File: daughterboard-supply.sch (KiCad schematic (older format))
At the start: 12 parts, among them J4 43045-1013, Q15 DMN4010LFG-7, U15 AP62301WU-7

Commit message: Loclib performed
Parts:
- Q15: footprint antmicro-footprints:POWERVDFN-8 -> nuc-compute-cluster-power-breakout-footprints:POWERVDFN-8; symbol antmicroTransistorsFETsMOSFETsSingle:DMN4010LFG-7 -> nuc-compute-cluster-power-breakout:DMN4010LFG-7
- R38, R39: footprint antmicro-footprints:0402-res -> nuc-compute-cluster-power-breakout-footprints:0402-res; symbol antmicroResistors0402:R_10k_0402 -> nuc-compute-cluster-power-breakout:R_10k_0402
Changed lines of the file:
@@
 DB_3V3
 $Comp
-L antmicroTransistorsFETsMOSFETsSingle:DMN4010LFG-7 Q15
+L nuc-compute-cluster-power-breakout:DMN4010LFG-7 Q15
 U 1 1 626C5C42
 P 3525 3950
 F 0 "Q15" V 3861 3950 79  0000 C CNN
 F 1 "DMN4010LFG-7" V 3726 3950 79  0000 C CNN
-F 2 "antmicro-footprints:POWERVDFN-8" H 3525 3950 79  0001 C CNN
+F 2 "nuc-compute-cluster-power-breakout-footprints:POWERVDFN-8" H 3525 3950 79  0001 C CNN
 F 3 "https://www.diodes.com/assets/Datasheets/DMN4010LFG.pdf" H 3525 3950 79  0001 C CNN
 F 4 "DMN4010LFG-7" H 3525 3950 79  0001 C CNN "MPN"
@@
 $EndComp
 $Comp
-L antmicroResistors0402:R_10k_0402 R38
+L nuc-compute-cluster-power-breakout:R_10k_0402 R38
 U 1 1 626D757A
 P 3625 4500
 F 0 "R38" V 3575 4325 60  0000 L CNN
 F 1 "R_10k_0402" H 3625 4350 60  0001 C CNN
-F 2 "antmicro-footprints:0402-res" H 3825 4700 60  0001 L CNN
+F 2 "nuc-compute-cluster-power-breakout-footprints:0402-res" H 3825 4700 60  0001 L CNN
 F 3 "" H 3625 4500 50  0001 C CNN
 F 4 "VISHAY" H 3825 4900 60  0001 L CNN "Manufacturer"
@@
 	3875 3925 4050 3925
 $Comp
-L antmicroResistors0402:R_10k_0402 R39
+L nuc-compute-cluster-power-breakout:R_10k_0402 R39
 U 1 1 626D93ED
 P 3875 4500
 F 0 "R39" V 3825 4575 60  0000 L CNN
 F 1 "R_10k_0402" H 3875 4350 60  0001 C CNN
-F 2 "antmicro-footprints:0402-res" H 4075 4700 60  0001 L CNN
+F 2 "nuc-compute-cluster-power-breakout-footprints:0402-res" H 4075 4700 60  0001 L CNN
 F 3 "" H 3875 4500 50  0001 C CNN
 F 4 "VISHAY" H 4075 4900 60  0001 L CNN "Manufacturer"

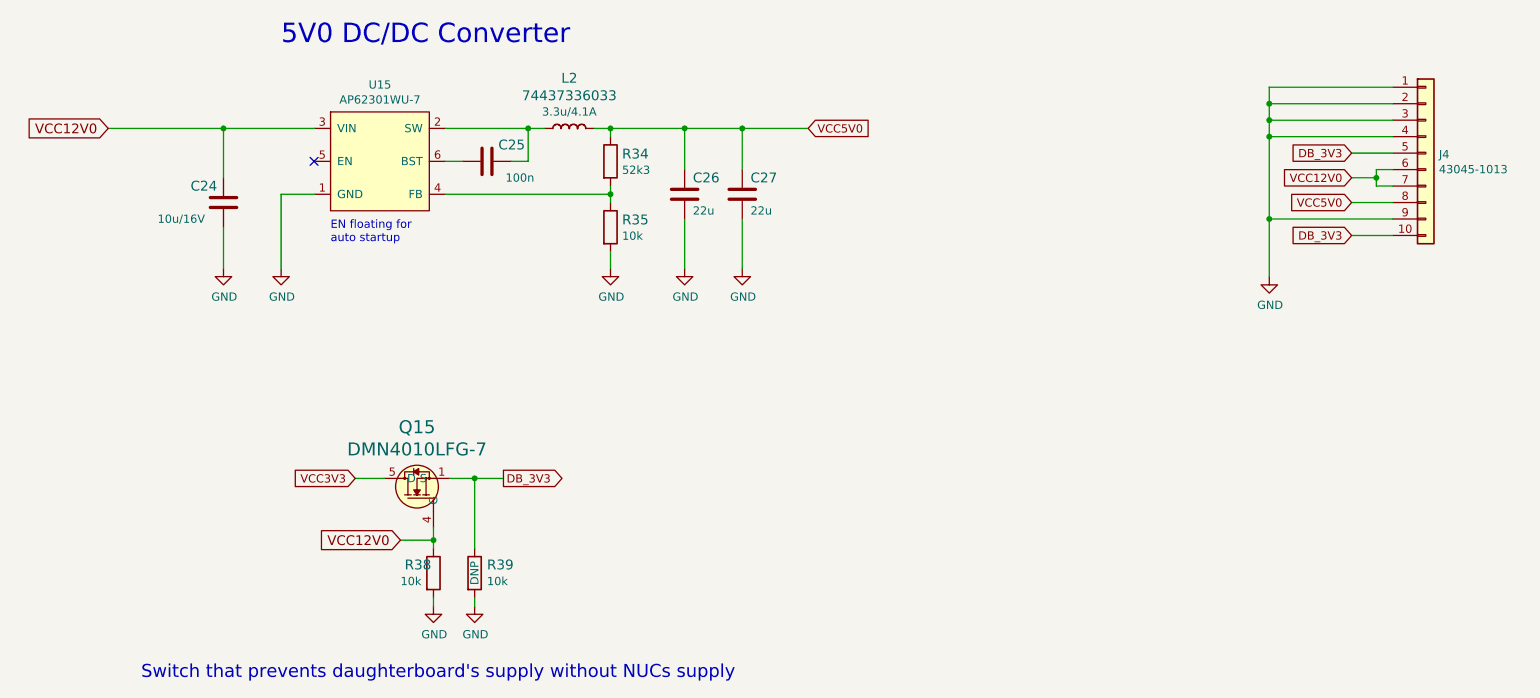
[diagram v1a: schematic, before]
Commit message: Galvanic isolation implementation
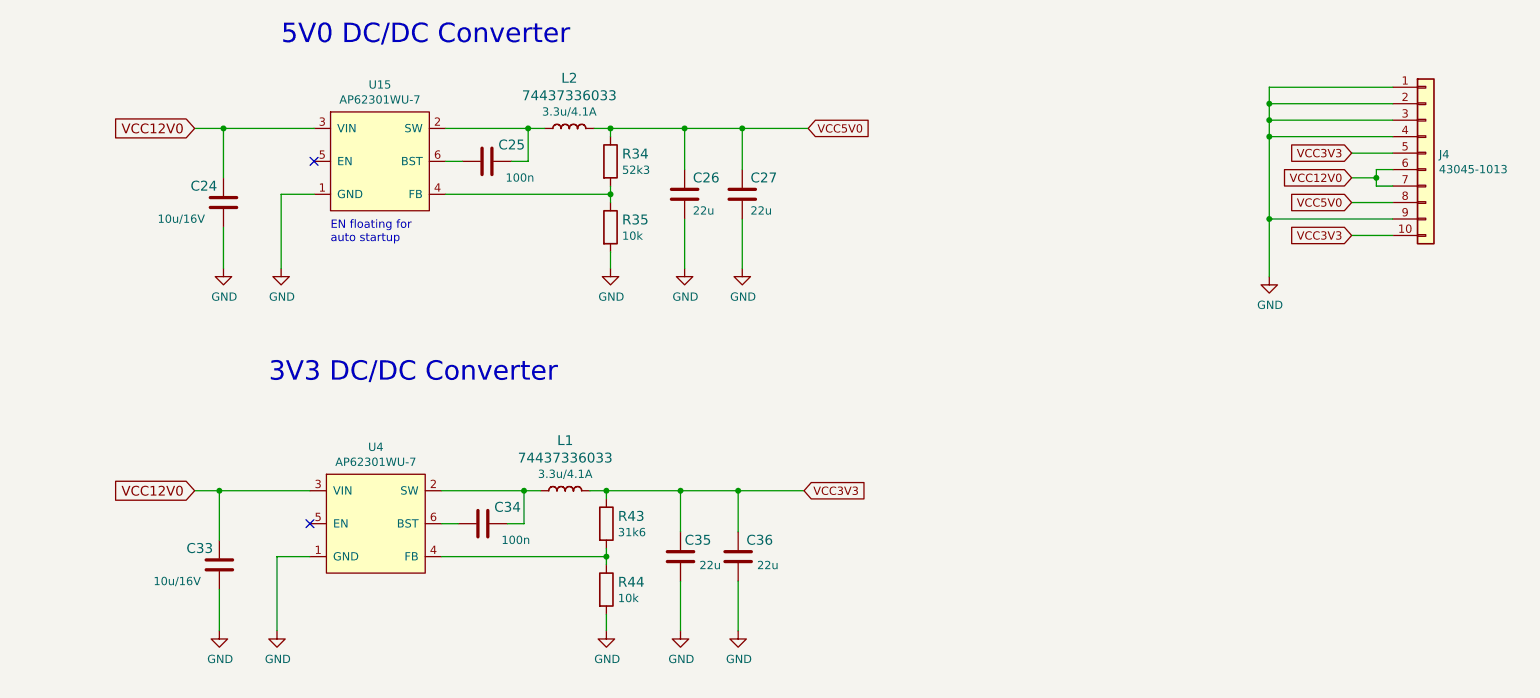
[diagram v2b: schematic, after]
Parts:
- removed Q15: DMN4010LFG-7, nuc-compute-cluster-power-breakout-footprints:POWERVDFN-8, symbol nuc-compute-cluster-power-breakout:DMN4010LFG-7
- removed R38, R39: R_10k_0402, nuc-compute-cluster-power-breakout-footprints:0402-res, symbol nuc-compute-cluster-power-breakout:R_10k_0402
- added C33: C_10u_16V_0603, nuc-compute-cluster-power-breakout-footprints:0603-cap, symbol nuc-compute-cluster-power-breakout:C_10u_16V_0603
- added C34: C_100n_0402, nuc-compute-cluster-power-breakout-footprints:0402-cap, symbol nuc-compute-cluster-power-breakout:C_100n_0402
- added C35, C36: C_22u_0603, nuc-compute-cluster-power-breakout-footprints:0603-cap, symbol nuc-compute-cluster-power-breakout:C_22u_0603
- added L1: 74437336033, nuc-compute-cluster-power-breakout-footprints:WE_74437336033, symbol nuc-compute-cluster-power-breakout:74437336033
- added R43: R_31k6_0402, nuc-compute-cluster-power-breakout-footprints:0402-res, symbol nuc-compute-cluster-power-breakout:R_31k6_0402
- added R44: R_10k_0402, nuc-compute-cluster-power-breakout-footprints:0402-res, symbol nuc-compute-cluster-power-breakout:R_10k_0402
- added U4: AP62301WU-7, nuc-compute-cluster-power-breakout-footprints:TSOT23-6, symbol nuc-compute-cluster-power-breakout:AP62301WU-7
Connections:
- net DB_3V3 is gone; now on net VCC3V3: J4.10 (Pin_10), J4.5 (Pin_5)
- net GND: now also C33.2, C35.2, C36.2, R44.2, U4.1 (GND)
- net VCC12V0: now also C33.1, U4.3 (VIN)
- net VCC3V3: now also C35.1, C36.1, L1.2 (P), R43.1
- new net: C34.1, L1.1 (P), U4.2 (SW)
- new net: R43.2, R44.1, U4.4 (FB)
- new net: C34.2, U4.6 (BST)
- no-connect marks 1 -> 2
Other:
- note added: "3V3 DC/DC Converter"
- note removed: "Switch that prevents daughterboard's supply without NUCs supply"
